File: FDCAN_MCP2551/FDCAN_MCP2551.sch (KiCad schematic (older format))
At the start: 4 parts, among them J1 Conn_01x06_Male, U1 MCP2551-I-SN

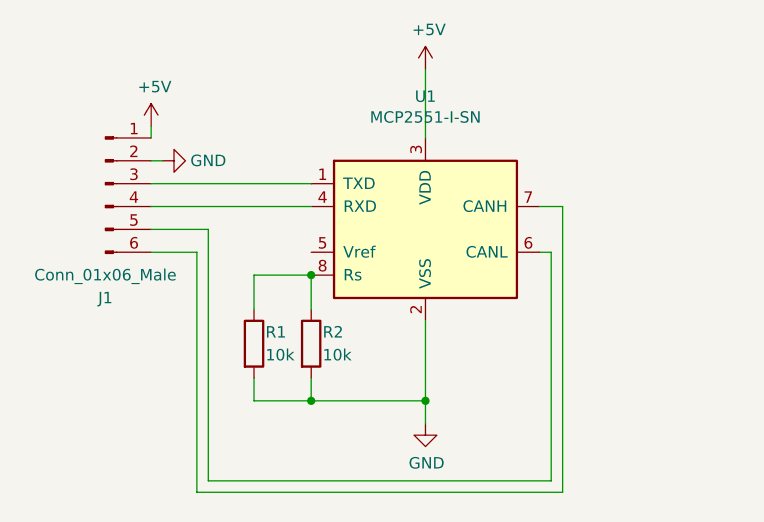
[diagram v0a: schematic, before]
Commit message: esqueatico circuito BMS para monitoramento de temperatura
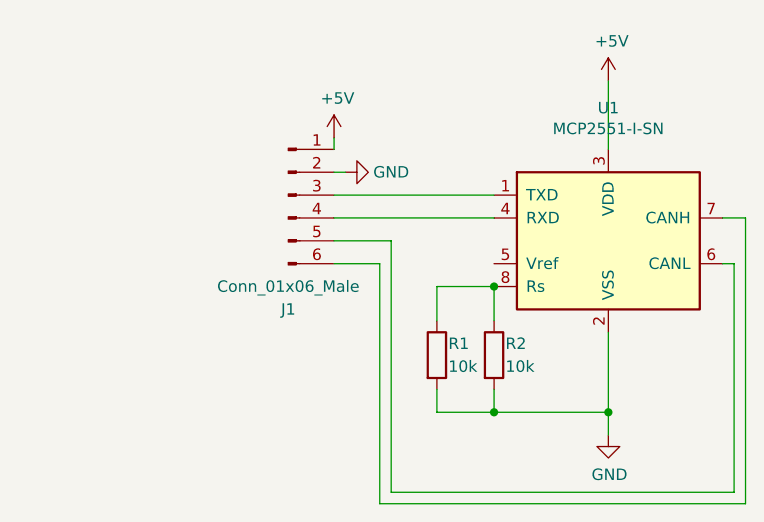
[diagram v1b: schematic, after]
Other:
- moved on the sheet: J1, R1, R2, U1
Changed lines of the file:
@@
 L power:+5V #PWR0101
 U 1 1 6008878A
-P 4950 2350
-F 0 "#PWR0101" H 4950 2200 50  0001 C CNN
-F 1 "+5V" H 4965 2523 50  0000 C CNN
-F 2 "" H 4950 2350 50  0001 C CNN
-F 3 "" H 4950 2350 50  0001 C CNN
-	1    4950 2350
+P 5750 2400
+F 0 "#PWR0101" H 5750 2250 50  0001 C CNN
+F 1 "+5V" H 5765 2573 50  0000 C CNN
+F 2 "" H 5750 2400 50  0001 C CNN
+F 3 "" H 5750 2400 50  0001 C CNN
+	1    5750 2400
 	1    0    0    -1
 $EndComp
@@
 L Connector:Conn_01x06_Male J1
 U 1 1 6008B043
-P 3550 2850
-F 0 "J1" H 3550 2350 50  0000 C CNN
-F 1 "Conn_01x06_Male" H 3550 2450 50  0000 C CNN
-F 2 "Connector_PinHeader_2.54mm:PinHeader_1x06_P2.54mm_Vertical" H 3550 2850 50  0001 C CNN
-F 3 "~" H 3550 2850 50  0001 C CNN
-	1    3550 2850
+P 4350 2900
+F 0 "J1" H 4350 2400 50  0000 C CNN
+F 1 "Conn_01x06_Male" H 4350 2500 50  0000 C CNN
+F 2 "Connector_PinHeader_2.54mm:PinHeader_1x06_P2.54mm_Vertical" H 4350 2900 50  0001 C CNN
+F 3 "~" H 4350 2900 50  0001 C CNN
+	1    4350 2900
 	1    0    0    -1
 $EndComp
@@
 L power:+5V #PWR0102
 U 1 1 6008D119
-P 3750 2600
-F 0 "#PWR0102" H 3750 2450 50  0001 C CNN
-F 1 "+5V" H 3765 2773 50  0000 C CNN
-F 2 "" H 3750 2600 50  0001 C CNN
-F 3 "" H 3750 2600 50  0001 C CNN
-	1    3750 2600
+P 4550 2650
+F 0 "#PWR0102" H 4550 2500 50  0001 C CNN
+F 1 "+5V" H 4565 2823 50  0000 C CNN
+F 2 "" H 4550 2650 50  0001 C CNN
+F 3 "" H 4550 2650 50  0001 C CNN
+	1    4550 2650
 	1    0    0    -1
 $EndComp
 Wire Wire Line
-	3750 2650 3750 2600
+	4550 2700 4550 2650
 $Comp
 L Device:R R2
 U 1 1 60094D85
-P 4450 3550
-F 0 "R2" H 4500 3600 50  0000 L CNN
-F 1 "10k" H 4500 3500 50  0000 L CNN
-F 2 "Resistor_SMD:R_0805_2012Metric" V 4380 3550 50  0001 C CNN
-F 3 "~" H 4450 3550 50  0001 C CNN
-	1    4450 3550
+P 5250 3600
+F 0 "R2" H 5300 3650 50  0000 L CNN
+F 1 "10k" H 5300 3550 50  0000 L CNN
+F 2 "Resistor_SMD:R_0805_2012Metric" V 5180 3600 50  0001 C CNN
+F 3 "~" H 5250 3600 50  0001 C CNN
+	1    5250 3600
 	1    0    0    -1
 $EndComp
 Wire Wire Line
-	4950 2350 4950 2650
+	5750 2400 5750 2700
 $Comp
 L power:GND #PWR0103
 U 1 1 600956DC
-P 4950 3900
-F 0 "#PWR0103" H 4950 3650 50  0001 C CNN
-F 1 "GND" H 4955 3727 50  0000 C CNN
-F 2 "" H 4950 3900 50  0001 C CNN
-F 3 "" H 4950 3900 50  0001 C CNN
-	1    4950 3900
+P 5750 3950
+F 0 "#PWR0103" H 5750 3700 50  0001 C CNN
+F 1 "GND" H 5755 3777 50  0000 C CNN
+F 2 "" H 5750 3950 50  0001 C CNN
+F 3 "" H 5750 3950 50  0001 C CNN
+	1    5750 3950
 	1    0    0    -1
 $EndComp
 Wire Wire Line
-	4950 3450 4950 3800
+	5750 3500 5750 3850
 Wire Wire Line
-	4450 3400 4450 3250
+	5250 3450 5250 3300
 Wire Wire Line
-	4450 3700 4450 3800
+	5250 3750 5250 3850
 Wire Wire Line
-	4450 3800 4950 3800
+	5250 3850 5750 3850
 Wire Wire Line
-	4950 3900 4950 3800
-Connection ~ 4950 3800
+	5750 3950 5750 3850
+Connection ~ 5750 3850
 $Comp
 L Device:R R1
 U 1 1 60097110
-P 4200 3550
-F 0 "R1" H 4250 3600 50  0000 L CNN
-F 1 "10k" H 4250 3500 50  0000 L CNN
-F 2 "Resistor_SMD:R_0805_2012Metric" V 4130 3550 50  0001 C CNN
-F 3 "~" H 4200 3550 50  0001 C CNN
-	1    4200 3550
+P 5000 3600
+F 0 "R1" H 5050 3650 50  0000 L CNN
+F 1 "10k" H 5050 3550 50  0000 L CNN
+F 2 "Resistor_SMD:R_0805_2012Metric" V 4930 3600 50  0001 C CNN
+F 3 "~" H 5000 3600 50  0001 C CNN
+	1    5000 3600
 	1    0    0    -1
 $EndComp
 Wire Wire Line
-	4200 3400 4200 3250
+	5000 3450 5000 3300
 Wire Wire Line
-	4200 3250 4450 3250
+	5000 3300 5250 3300
 Wire Wire Line
-	4200 3700 4200 3800
+	5000 3750 5000 3850
 Wire Wire Line
-	4200 3800 4450 3800
-Connection ~ 4450 3800
+	5000 3850 5250 3850
+Connection ~ 5250 3850
 Wire Wire Line
-	3750 2850 4450 2850
+	4550 2900 5250 2900
 Wire Wire Line
-	3750 2950 4450 2950
+	4550 3000 5250 3000
 Wire Wire Line
-	3750 3050 4000 3050
+	4550 3100 4800 3100
 Wire Wire Line
-	3950 3150 3750 3150
-Connection ~ 4450 3250
+	4750 3200 4550 3200
+Connection ~ 5250 3300
 $Comp
 L Interface_CAN_LIN:MCP2551-I-SN U1
 U 1 1 60087AEF
-P 4950 3050
-F 0 "U1" H 4950 3631 50  0000 C CNN
-F 1 "MCP2551-I-SN" H 4950 3540 50  0000 C CNN
-F 2 "Package_SO:SOIC-8_3.9x4.9mm_P1.27mm" H 4950 2550 50  0001 C CIN
-F 3 "http://ww1.microchip.com/downloads/en/devicedoc/21667d.pdf" H 4950 3050 50  0001 C CNN
-	1    4950 3050
+P 5750 3100
+F 0 "U1" H 5750 3681 50  0000 C CNN
+F 1 "MCP2551-I-SN" H 5750 3590 50  0000 C CNN
+F 2 "Package_SO:SOIC-8_3.9x4.9mm_P1.27mm" H 5750 2600 50  0001 C CIN
+F 3 "http://ww1.microchip.com/downloads/en/devicedoc/21667d.pdf" H 5750 3100 50  0001 C CNN
+	1    5750 3100
 	1    0    0    -1
 $EndComp
 Wire Wire Line
-	3950 4200 3950 3150
+	4750 4250 4750 3200
 Wire Wire Line
-	4000 3050 4000 4150
+	4800 3100 4800 4200
 Wire Wire Line
-	5500 4150 5500 3150
+	6300 4200 6300 3200
 Wire Wire Line
-	5500 3150 5450 3150
+	6300 3200 6250 3200
 Wire Wire Line
-	4000 4150 5500 4150
+	4800 4200 6300 4200
 Wire Wire Line
-	3950 4200 5550 4200
+	4750 4250 6350 4250
 Wire Wire Line
-	5550 4200 5550 2950
+	6350 4250 6350 3000
 Wire Wire Line
-	5550 2950 5450 2950
+	6350 3000 6250 3000
 $Comp
 L power:GND #PWR0104
 U 1 1 600A661F
-P 3800 2750
-F 0 "#PWR0104" H 3800 2500 50  0001 C CNN
-F 1 "GND" V 3800 2550 50  0000 C CNN
-F 2 "" H 3800 2750 50  0001 C CNN
-F 3 "" H 3800 2750 50  0001 C CNN
-	1    3800 2750
+P 4600 2800
+F 0 "#PWR0104" H 4600 2550 50  0001 C CNN
+F 1 "GND" V 4600 2600 50  0000 C CNN
+F 2 "" H 4600 2800 50  0001 C CNN
+F 3 "" H 4600 2800 50  0001 C CNN
+	1    4600 2800
 	0    -1   -1   0
 $EndComp
 Wire Wire Line
-	3750 2750 3800 2750
+	4550 2800 4600 2800
 $EndSCHEMATC
